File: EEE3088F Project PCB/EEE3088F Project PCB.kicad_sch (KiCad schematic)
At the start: 15 parts, among them J1 JST PH 2.00mm connector, U1 DRV8833PWR, U2 DRV8833PWPR, U3 INA219AxD

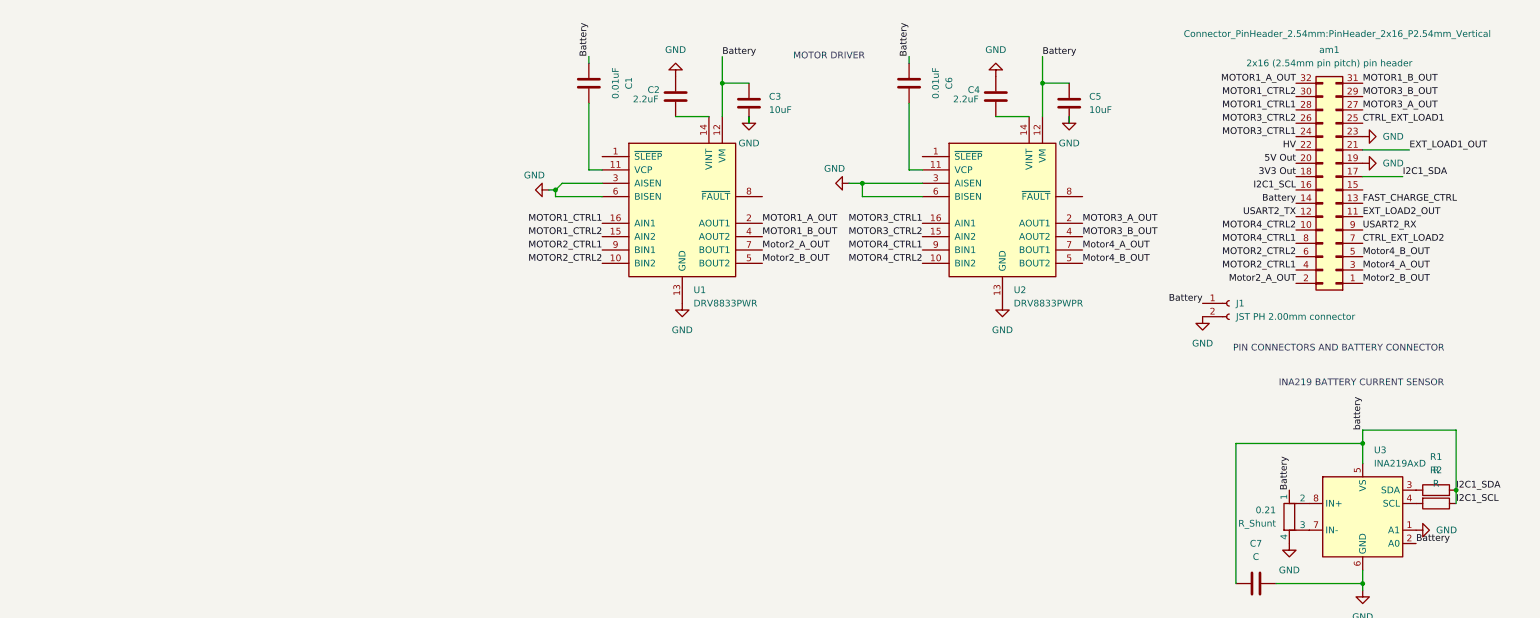
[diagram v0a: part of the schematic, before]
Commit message: added usb c integration with footprints
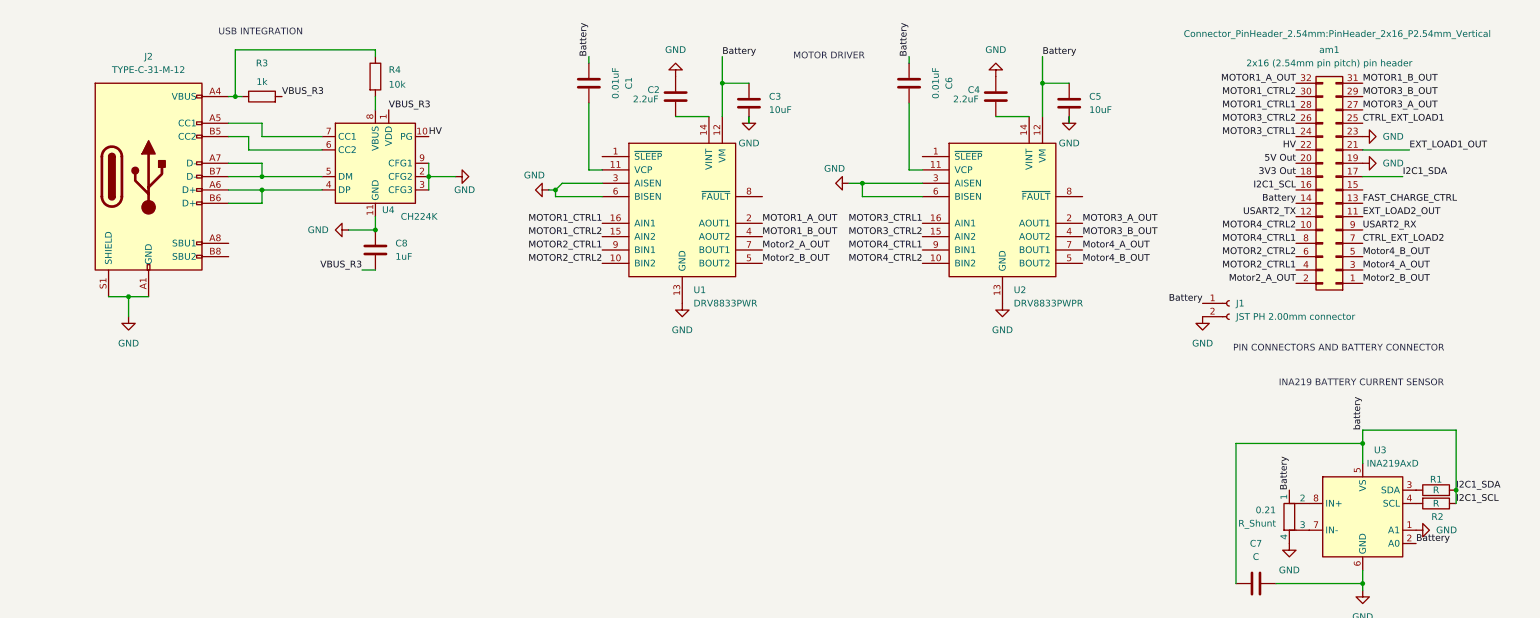
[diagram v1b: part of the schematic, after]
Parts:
- added C8: 1uF, exported_footprints:CAPC3216X180N, symbol Device:C
- added J2: TYPE-C-31-M-12, exported_footprints:HRO_TYPE-C-31-M-12, symbol Connector:USB_C_Receptacle_USB2.0_16P
- added R3: 1k, exported_footprints:RESC3115X65N, symbol Device:R
- added R4: 10k, exported_footprints:RESC3115X65N, symbol Device:R
- added U4: CH224K, Package_SO:SSOP-10-1EP_3.9x4.9mm_P1mm_EP2.1x3.3mm, symbol Interface_USB:CH224K
- C1, C6: footprint (none) -> exported_footprints:CAPC2012X140N
- C2, C4: footprint (none) -> exported_footprints:CAPC1608X90N
- C3, C5: footprint (none) -> exported_footprints:CAPC1005X55N
- U1, U2: footprint Package_SO:HTSSOP-16-1EP_4.4x5mm_P0.65mm_EP3.4x5mm_Mask2.46x2.31mm_ThermalVias -> exported_footprints:SOP65P640X120-16N
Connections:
- net GND: now also C8.2, J2.A1 (GND), J2.A12 (GND), J2.B1 (GND), J2.B12 (GND), J2.S1 (SHIELD), U4.11 (GND), U4.2 (CFG2), U4.3 (CFG3), U4.9 (CFG1)
- net HV: now also U4.10 (PG)
- new net: J2.A4 (VBUS), J2.A9 (VBUS), J2.B4 (VBUS), J2.B9 (VBUS), R3.1, R4.1
- new net: J2.A5 (CC1), U4.7 (CC1)
- new net: J2.A6 (D+), J2.B6 (D+), U4.4 (DP)
- new net: J2.A7 (D-), J2.B7 (D-), U4.5 (DM)
- new net: J2.B5 (CC2), U4.6 (CC2)
- new net: R4.2, U4.8 (VBUS)
- new net VBUS_R3: C8.1, R3.2, U4.1 (VDD)
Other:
- note added: "USB INTEGRATION"

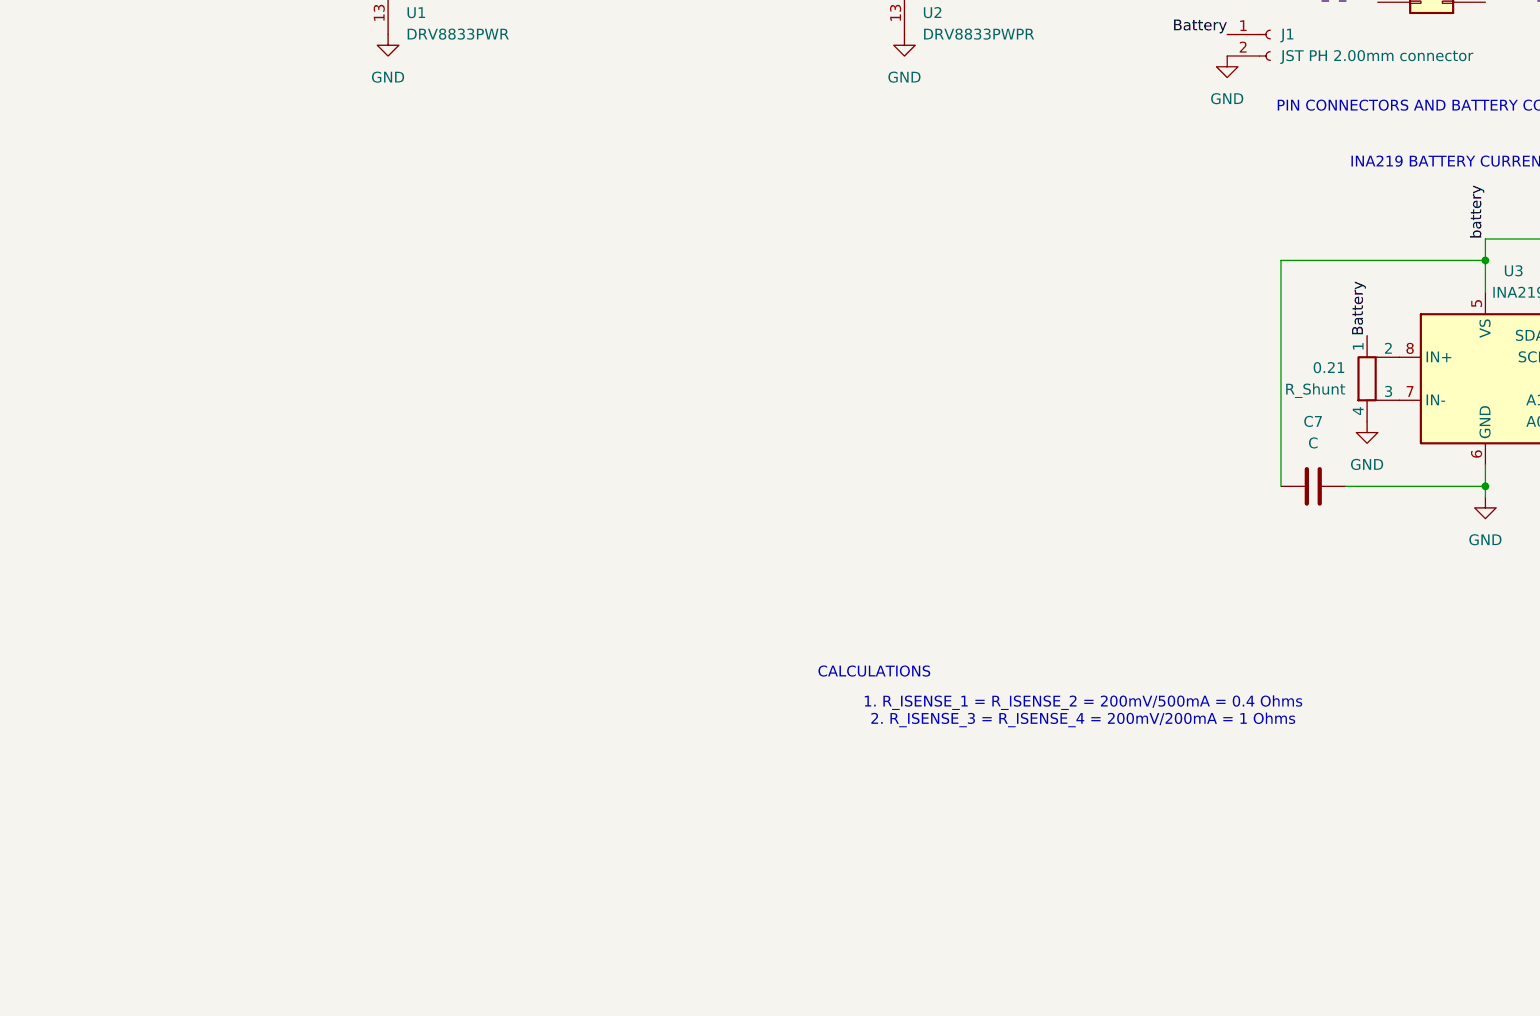
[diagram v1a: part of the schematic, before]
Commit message: added regulatores, updated outputs, added on/off switch
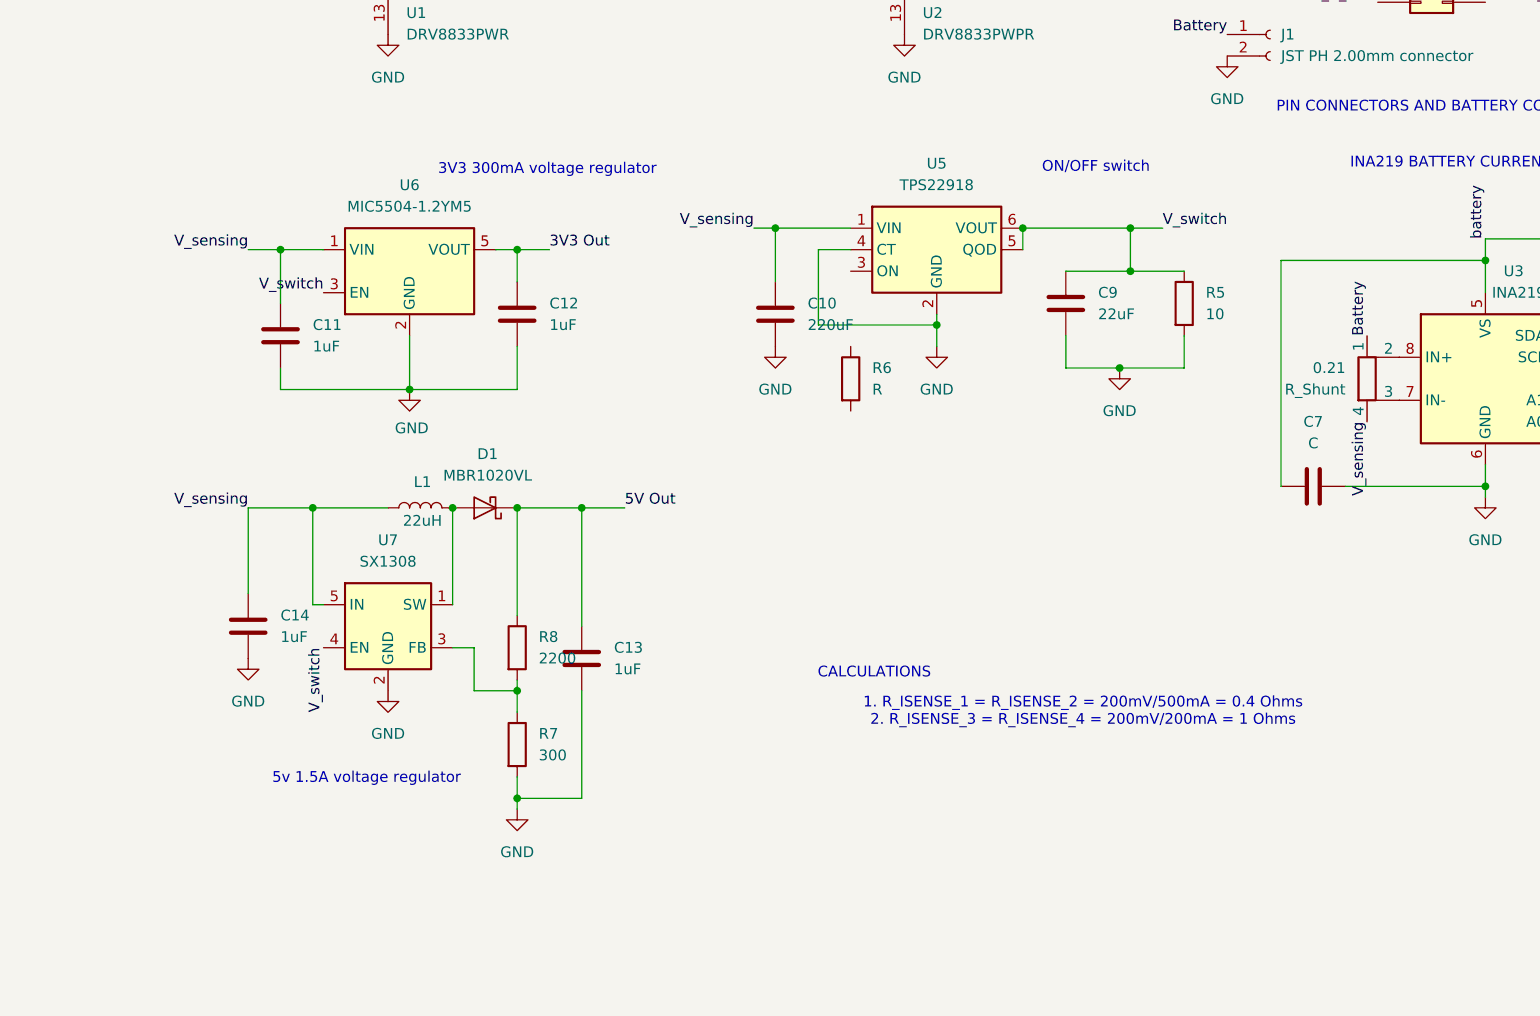
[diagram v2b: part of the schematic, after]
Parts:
- added C10: 220uF, symbol Device:C
- added C11, C12, C13, C14: 1uF, symbol Device:C
- added C9: 22uF, symbol Device:C
- added D1: MBR1020VL, Diode_SMD:D_SOD-123F, symbol Diode:MBR1020VL
- added L1: 22uH, symbol Device:L
- added R5: 10, symbol Device:R
- added R6: R, symbol Device:R
- added R7: 300, symbol Device:R
- added R8: 2200, symbol Device:R
- added U5: TPS22918, Package_TO_SOT_SMD:SOT-23-6, symbol Power_Management:TPS22917DBV
- added U6: MIC5504-1.2YM5, Package_TO_SOT_SMD:SOT-23-5, symbol Regulator_Linear:MIC5504-1.2YM5
- added U7: SX1308, Package_TO_SOT_SMD:SOT-23-6, symbol Regulator_Switching:MT3608
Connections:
- net 3V3 Out: now also C12.1, U6.5 (VOUT)
- net 5V Out: now also C13.1, D1.1 (K), R8.1
- net GND: now also C10.2, C11.2, C12.2, C13.2, C14.2, C9.2, R5.2, R7.2, U5.2 (GND), U5.4 (CT), U6.2 (GND), U7.2 (GND); no longer 0.21.4
- new net: R7.1, R8.2, U7.3 (FB)
- new net: D1.2 (A), L1.2, U7.1 (SW)
- new net V_sensing: 0.21.4, C10.1, C11.1, C14.1, L1.1, U5.1 (VIN), U6.1 (VIN), U7.5 (IN)
- new net V_switch: C9.1, R5.1, U5.5 (QOD), U5.6 (VOUT), U6.3 (EN), U7.4 (EN)
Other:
- note added: "3V3 300mA voltage regulator"
- note added: "5v 1.5A voltage regulator"
- note added: "ON/OFF switch"

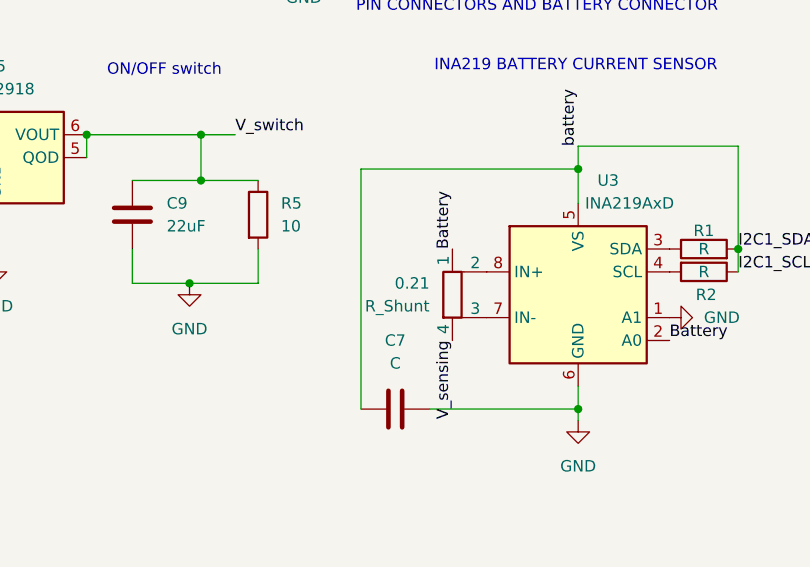
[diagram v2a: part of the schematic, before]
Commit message: adjusted shunt resistance
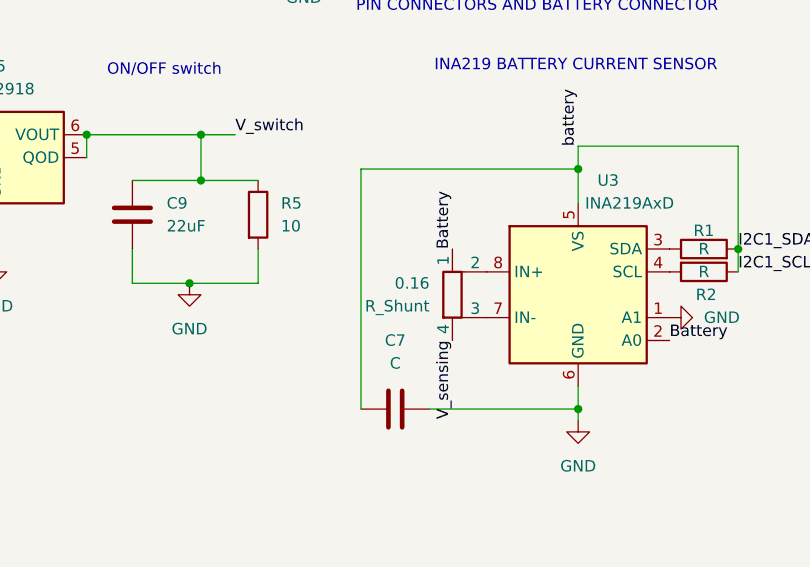
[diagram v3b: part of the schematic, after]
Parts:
- renumbered 0.21 to 0.16
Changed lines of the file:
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@@
 		(polyline
 			(pts
-				(xy 91.44 12.7) (xy 91.44 78.74) (xy 219.71 78.74) (xy 219.71 12.7)
+				(xy 228.6 78.74) (xy 228.6 127) (xy 284.48 127) (xy 284.48 81.28) (xy 281.94 78.74)
 			)
 			(stroke
@@
 		(polyline
 			(pts
-				(xy 12.7 12.7) (xy 12.7 78.74) (xy 91.44 78.74) (xy 91.44 12.7)
+				(xy 91.44 12.7) (xy 91.44 78.74) (xy 219.71 78.74) (xy 219.71 12.7)
 			)
 			(stroke
@@
 		(polyline
 			(pts
-				(xy 176.53 165.1) (xy 176.53 127) (xy 285.75 127) (xy 285.75 165.1) (xy 284.48 166.37) (xy 177.8 166.37)
+				(xy 12.7 12.7) (xy 12.7 78.74) (xy 91.44 78.74) (xy 91.44 12.7)
 			)
 			(stroke
@@
 		(polyline
 			(pts
-				(xy 228.6 78.74) (xy 228.6 127) (xy 284.48 127) (xy 284.48 81.28) (xy 281.94 78.74)
+				(xy 176.53 165.1) (xy 176.53 127) (xy 285.75 127) (xy 285.75 165.1) (xy 284.48 166.37) (xy 177.8 166.37)
 			)
 			(stroke
@@
 		(dnp no)
 		(fields_autoplaced yes)
-		(property "Reference" "0.21"
+		(property "Reference" "0.16"
 			(at 241.3 106.6799 0)
 			(effects
@@
 			(project ""
 				(path "/e48caec1-c218-420e-929b-e5099c9fb7b6"
-					(reference "0.21")
+					(reference "0.16")
 					(unit 1)
 				)
